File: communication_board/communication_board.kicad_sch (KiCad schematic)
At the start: 20 parts, among them J1 Conn_01x04_Socket, U1 FE1.1s, Y1 Crystal

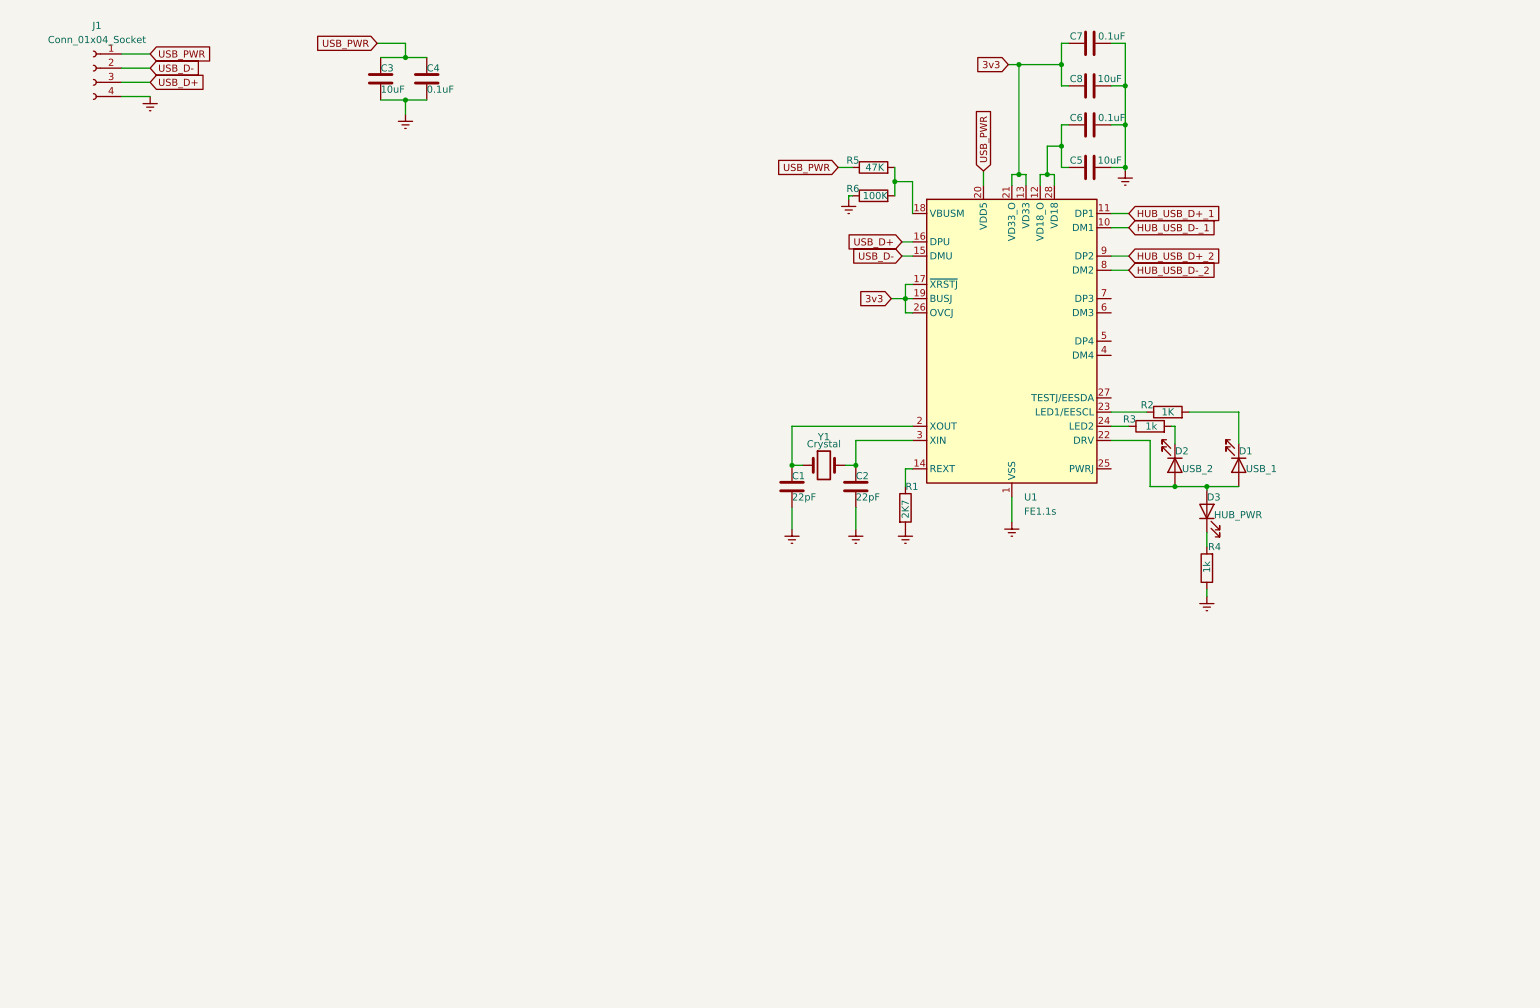
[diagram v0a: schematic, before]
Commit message: hub and imu tested at the same time
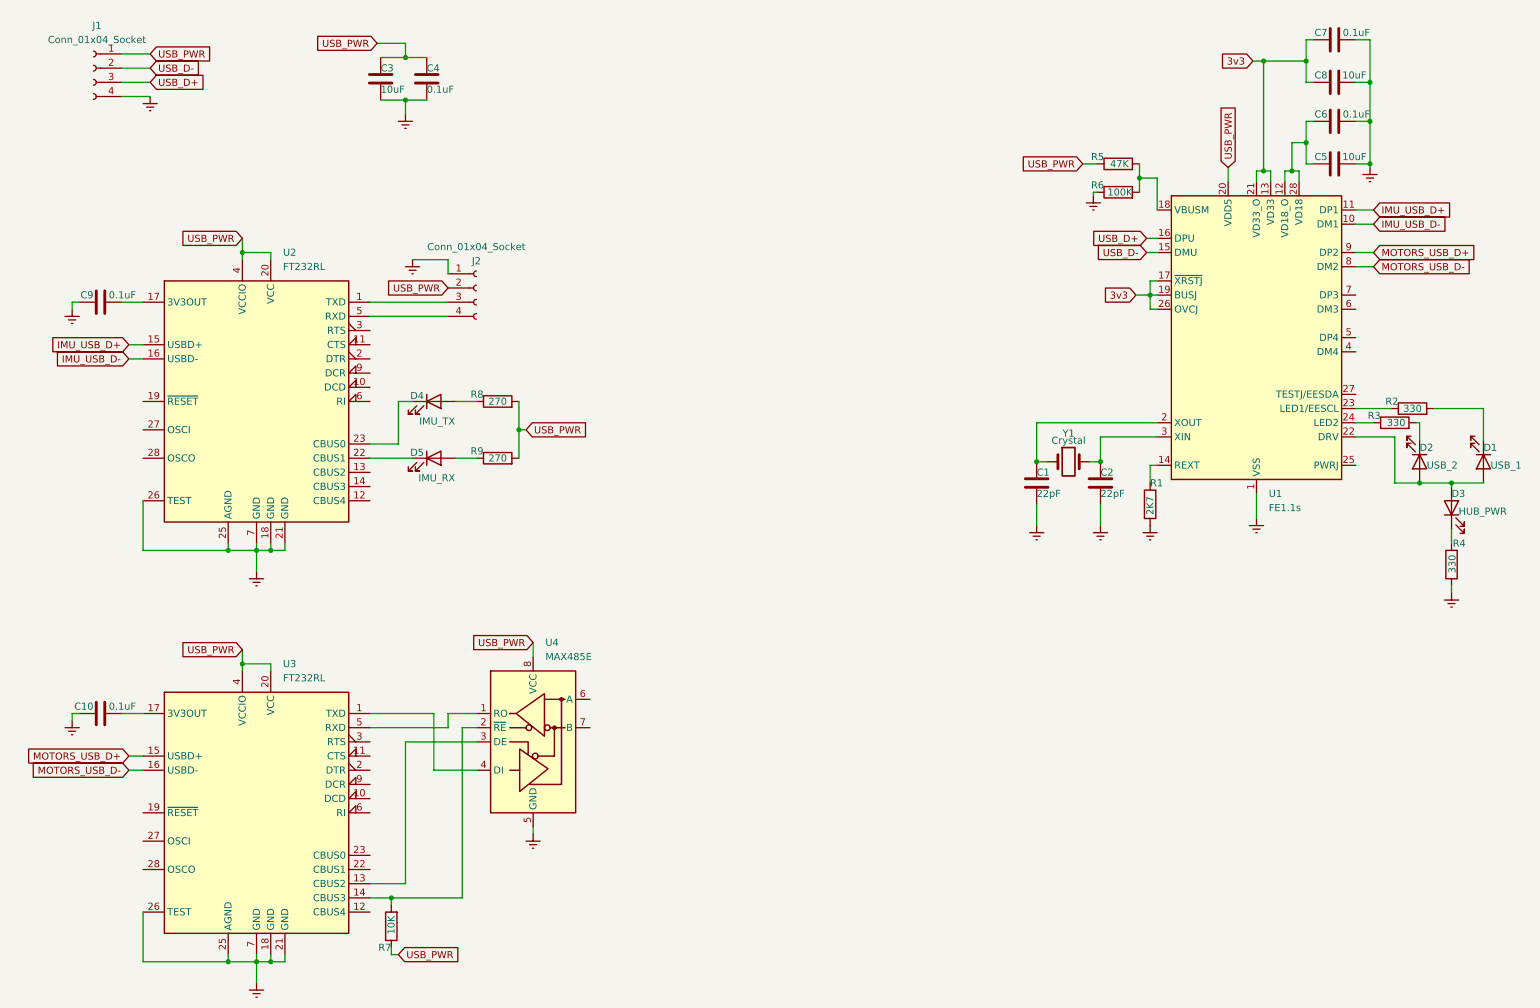
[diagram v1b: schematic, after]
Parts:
- added C10, C9: 0.1uF, Capacitor_SMD:C_1206_3216Metric, symbol Device:C
- added D4: IMU_TX, LED_SMD:LED_1206_3216Metric_Pad1.42x1.75mm_HandSolder, symbol Device:LED
- added D5: IMU_RX, LED_SMD:LED_1206_3216Metric_Pad1.42x1.75mm_HandSolder, symbol Device:LED
- added J2: Conn_01x04_Socket, Connector_PinHeader_2.54mm:PinHeader_1x04_P2.54mm_Vertical, symbol Connector:Conn_01x04_Socket
- added R7: 10K, Resistor_SMD:R_1206_3216Metric, symbol Device:R
- added R8, R9: 270, Resistor_SMD:R_1206_3216Metric, symbol Device:R
- added U2, U3: FT232RL, Package_SO:SSOP-28_5.3x10.2mm_P0.65mm, symbol Interface_USB:FT232RL
- added U4: MAX485E, Package_SO:SOIC-8_3.9x4.9mm_P1.27mm, symbol Interface_UART:MAX485E
- D1, D2, D3: footprint (none) -> LED_SMD:LED_1206_3216Metric_Pad1.42x1.75mm_HandSolder
- J1: footprint (none) -> Connector_PinHeader_2.54mm:PinHeader_1x04_P2.54mm_Vertical
- R2: value 1K -> 330
- R3, R4: value 1k -> 330
- Y1: footprint (none) -> components:ECS120185PXGMTR
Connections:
- net GNDREF: now also C10.1, C9.1, J2.1 (Pin_1), U2.18 (GND), U2.21 (GND), U2.25 (AGND), U2.26 (TEST), U2.7 (GND), U3.18 (GND), U3.21 (GND), U3.25 (AGND), U3.26 (TEST), U3.7 (GND), U4.5 (GND)
- net USB_PWR: now also J2.2 (Pin_2), R7.1, R8.2, R9.2, U2.20 (VCC), U2.4 (VCCIO), U3.20 (VCC), U3.4 (VCCIO), U4.8 (VCC)
- net HUB_USB_D+_1 renamed IMU_USB_D+
- net IMU_USB_D+: now also U2.15 (USBD+)
- net HUB_USB_D+_2 renamed MOTORS_USB_D+
- net MOTORS_USB_D+: now also U3.15 (USBD+)
- net HUB_USB_D-_1 renamed IMU_USB_D-
- net IMU_USB_D-: now also U2.16 (USBD-)
- net HUB_USB_D-_2 renamed MOTORS_USB_D-
- net MOTORS_USB_D-: now also U3.16 (USBD-)
- new net: C9.2, U2.17 (3V3OUT)
- new net: D4.2 (A), R8.1
- new net: U3.1 (TXD), U4.4 (DI)
- new net: U3.13 (CBUS2), U4.3 (DE)
- new net: R7.2, U3.14 (CBUS3), U4.2 (~{RE})
- new net: C10.2, U3.17 (3V3OUT)
- new net: U3.5 (RXD), U4.1 (RO)
- new net: D5.2 (A), R9.1
- new net: J2.3 (Pin_3), U2.1 (TXD)
- new net: D5.1 (K), U2.22 (CBUS1)
- new net: D4.1 (K), U2.23 (CBUS0)
- new net: J2.4 (Pin_4), U2.5 (RXD)
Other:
- moved on the sheet: C1, C2, C5, C6, C7, C8, D1, D2, D3, R1, R2, R3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

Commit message: motors conversor almost ready for test
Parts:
- added D6: MTR_TX, LED_SMD:LED_1206_3216Metric_Pad1.42x1.75mm_HandSolder, symbol Device:LED
- added D7: MTR_RX, LED_SMD:LED_1206_3216Metric_Pad1.42x1.75mm_HandSolder, symbol Device:LED
- added R10, R11: 270, Resistor_SMD:R_1206_3216Metric, symbol Device:R
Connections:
- net USB_PWR: now also R10.2, R11.2
- net at U3.22 (CBUS1): now also D7.1 (K)
- net at U3.23 (CBUS0): now also D6.1 (K)
- new net: D7.2 (A), R11.1
- new net: D6.2 (A), R10.1
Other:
- moved on the sheet: U4

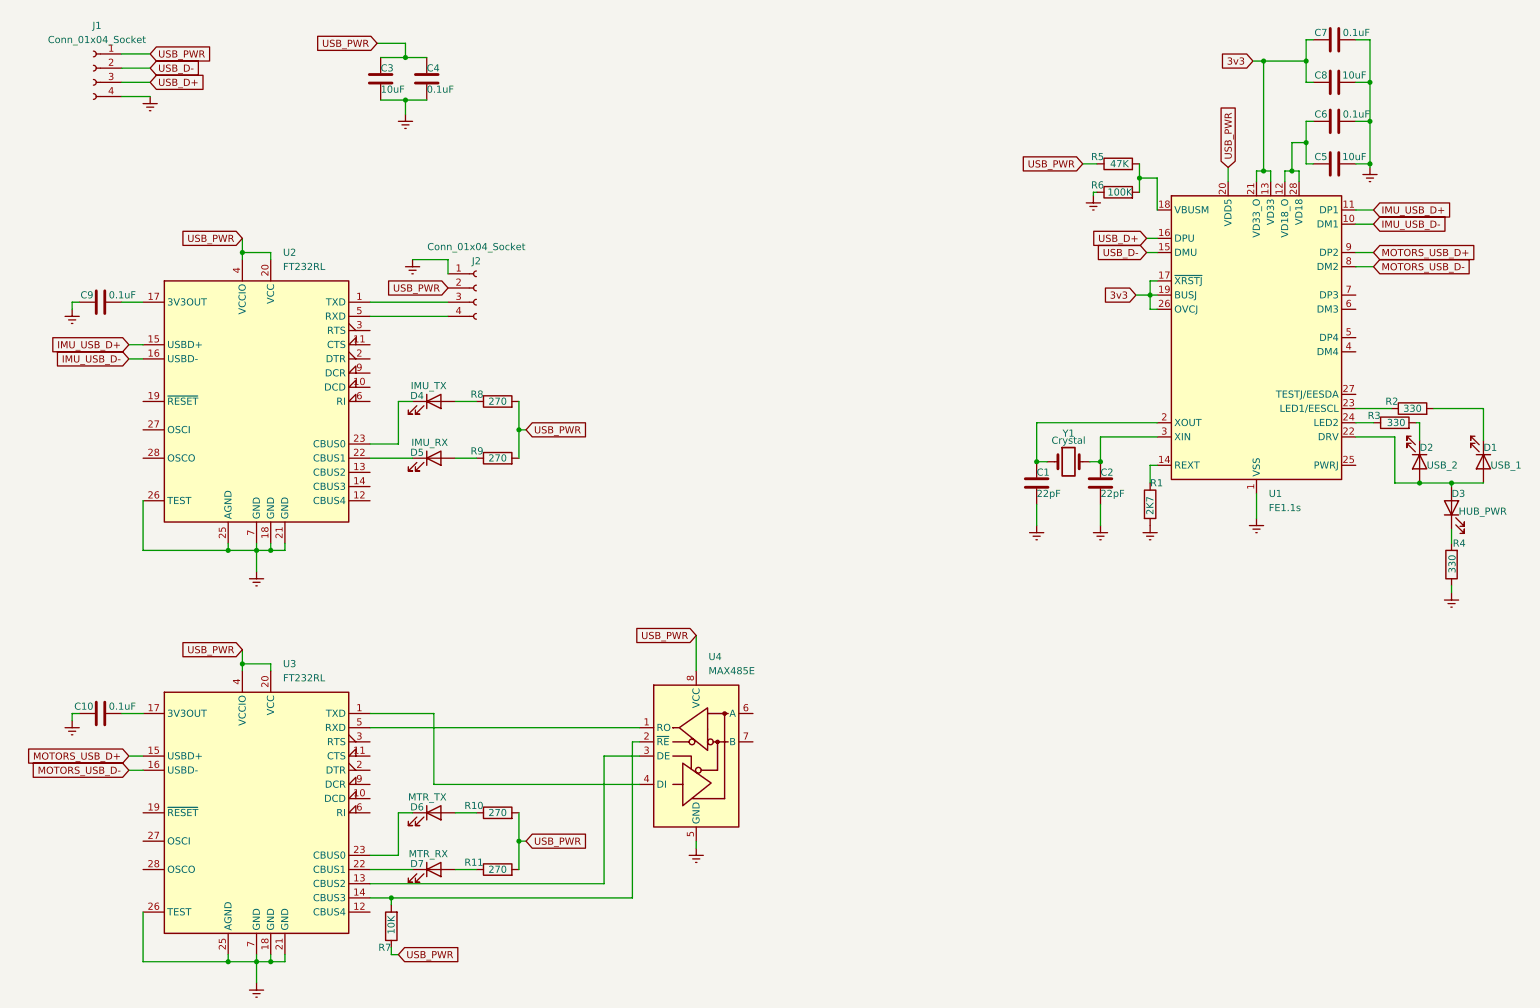
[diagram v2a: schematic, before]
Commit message: initial pcd components disposition
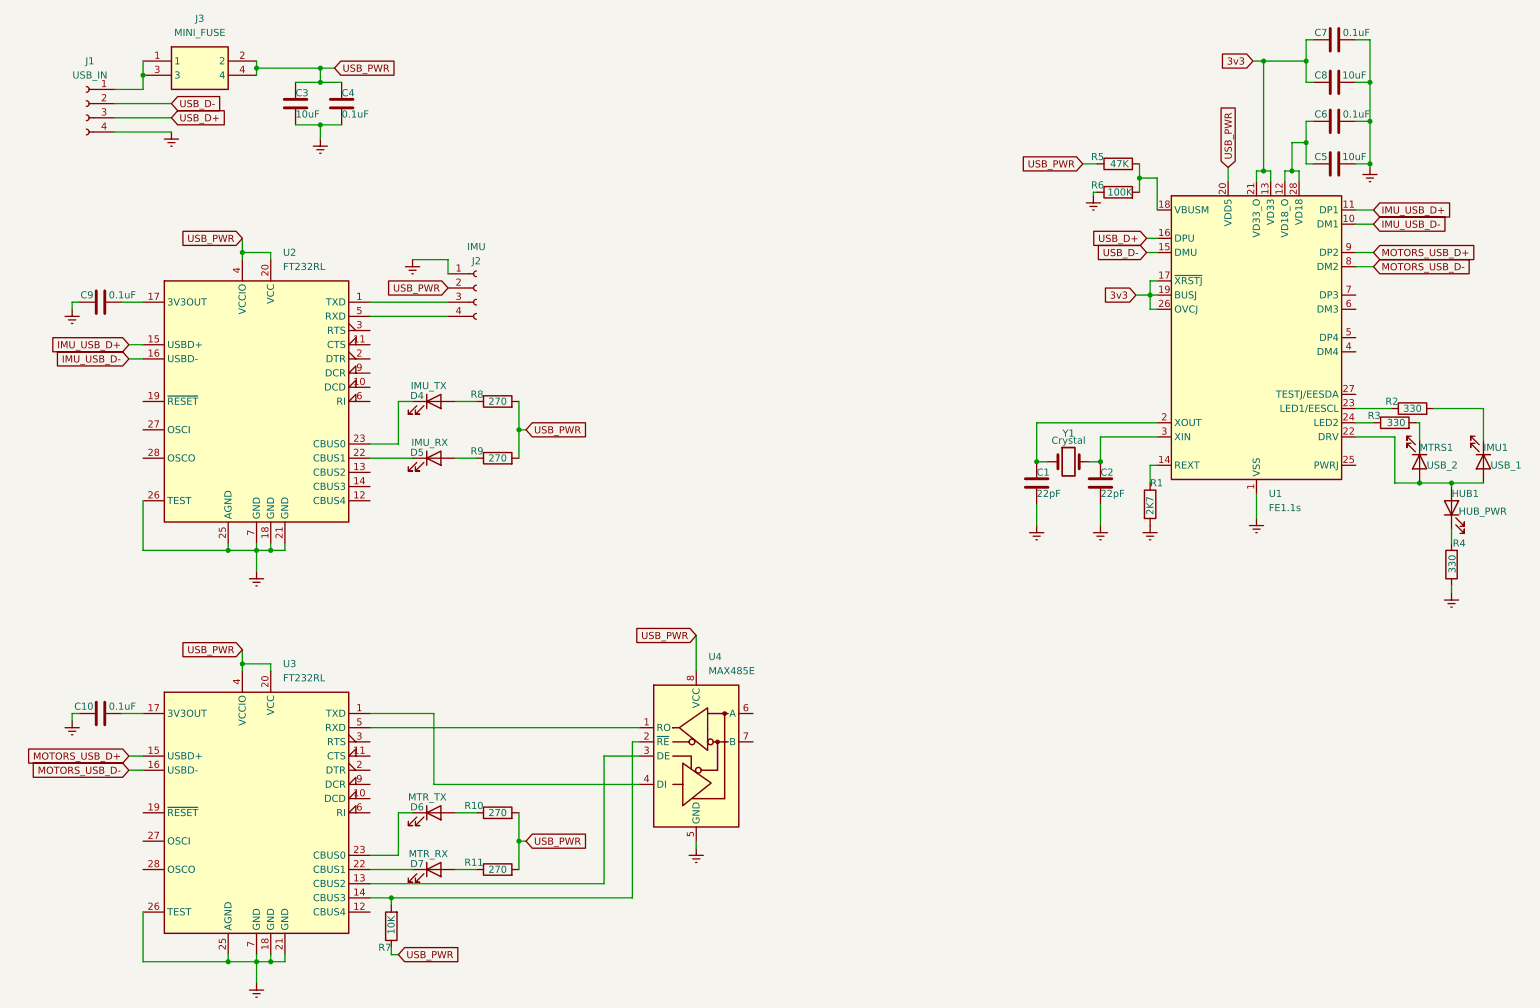
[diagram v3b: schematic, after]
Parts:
- added J3: MINI_FUSE, humanoid:MINI_FUSE, symbol humanoid:MINI_FUSE
- J1: value Conn_01x04_Socket -> USB_IN
- J2: value Conn_01x04_Socket -> IMU
- renumbered D3 to HUB1, D1 to IMU1, D2 to MTRS1
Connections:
- net USB_PWR: now also J3.2, J3.4; no longer J1.1 (Pin_1)
- new net: J1.1 (Pin_1), J3.1, J3.3
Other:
- moved on the sheet: C3, C4, J1

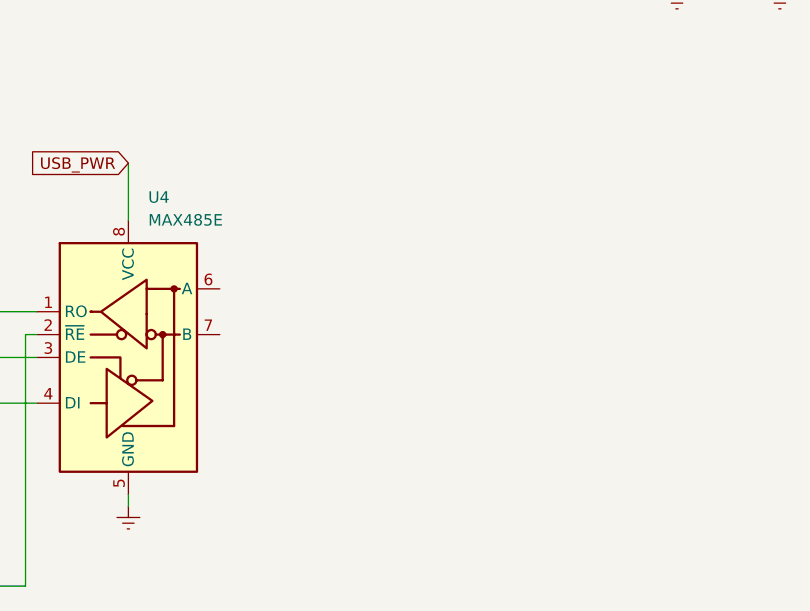
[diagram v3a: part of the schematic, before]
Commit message: communication board finished
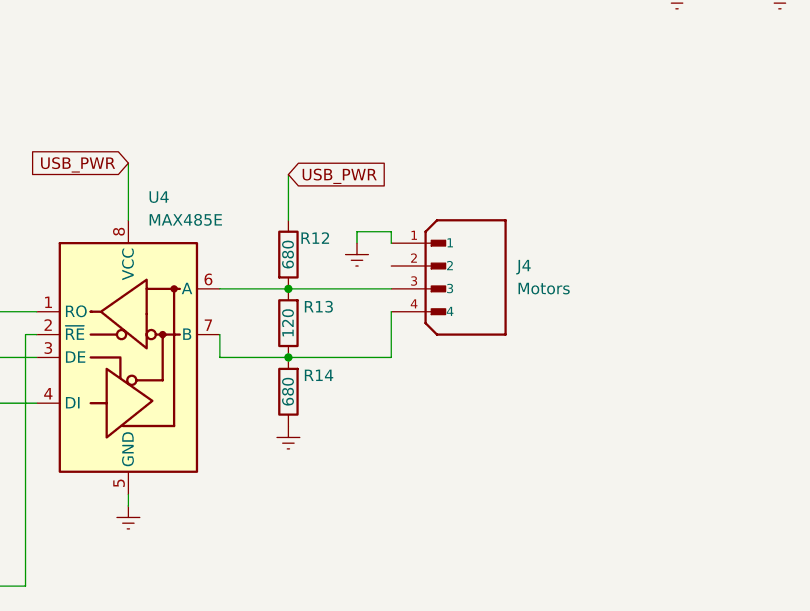
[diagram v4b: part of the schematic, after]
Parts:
- added J4: Motors, Connector_JST:JST_EH_B4B-EH-A_1x04_P2.50mm_Vertical, symbol humanoid:B4B-EH-A
- added R12, R14: 680, Resistor_SMD:R_1206_3216Metric, symbol Device:R
- added R13: 120, Resistor_SMD:R_1206_3216Metric, symbol Device:R
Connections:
- net GNDREF: now also J4.1, R14.1
- net USB_PWR: now also R12.1
- net at U4.6 (A): now also J4.3, R12.2, R13.2
- net at U4.7 (B): now also J4.4, R13.1, R14.2
